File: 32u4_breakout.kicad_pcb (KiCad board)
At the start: 2 copper layers, 40 x 80 mm, 15 parts, among them J1 ICSP, J8 PWR, J9 GND, U1 ATmega32U4-A, Y1 16 MHz

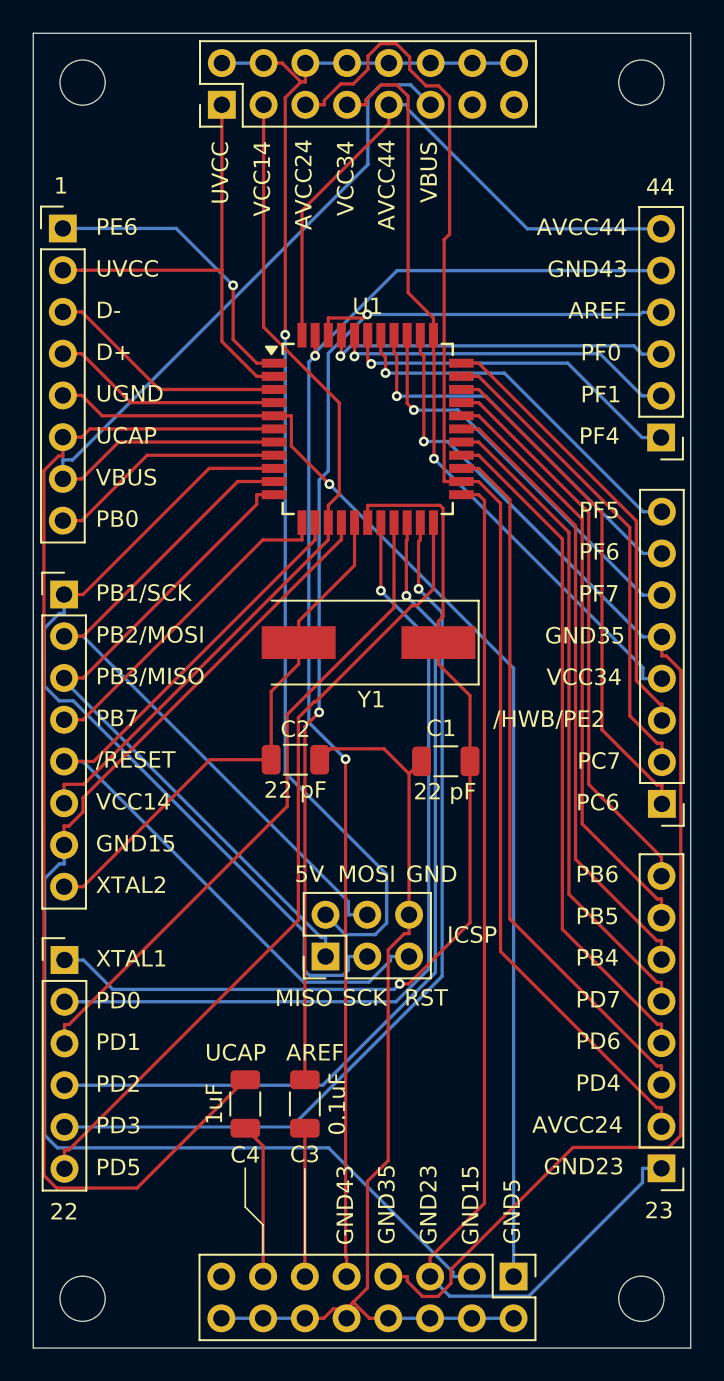
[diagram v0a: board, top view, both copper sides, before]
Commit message: Added LED for power and PC7/IO13
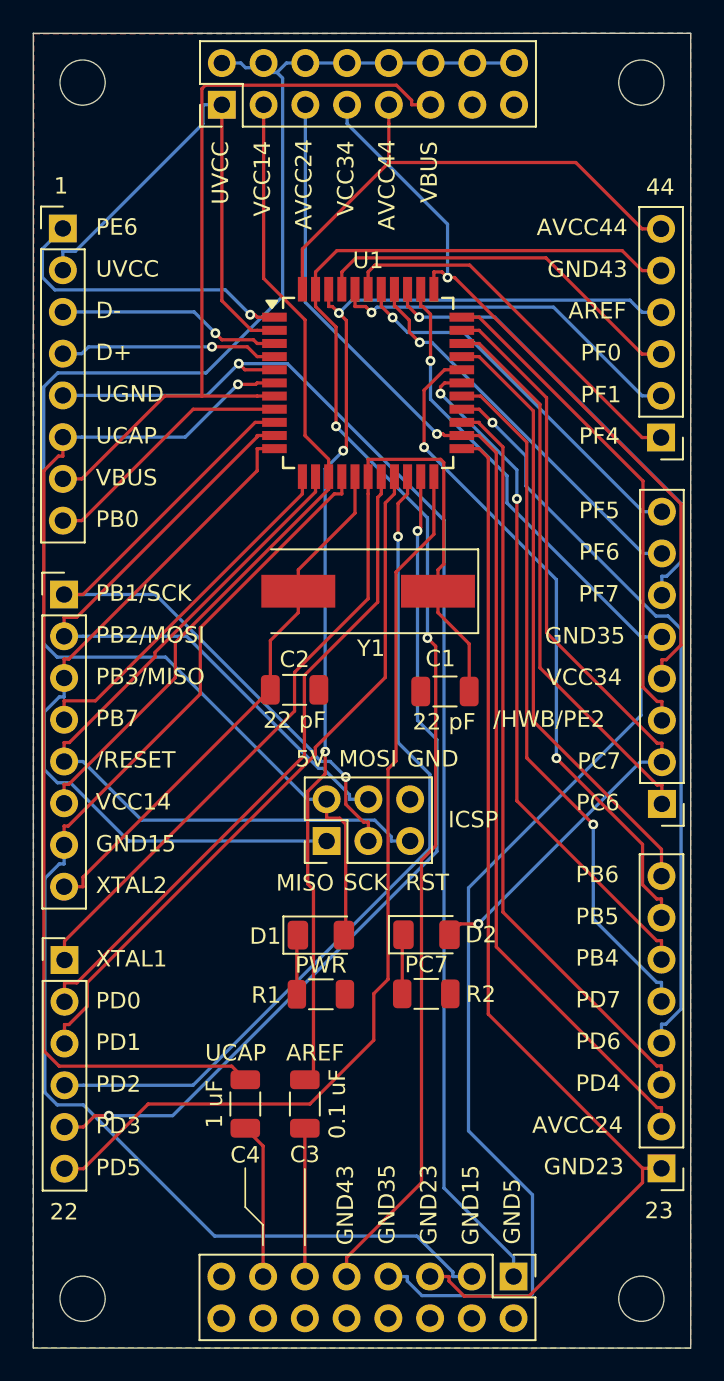
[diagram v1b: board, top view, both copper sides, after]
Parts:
- added D1: PWR, LED_SMD:LED_1206_3216Metric, F.Cu at (137.5, 94.9)
- added D2: PC7, LED_SMD:LED_1206_3216Metric, F.Cu at (143.9, 94.8)
- added R1: 220, Resistor_SMD:R_1206_3216Metric, F.Cu at (137.5, 98.5)
- added R2: 220, Resistor_SMD:R_1206_3216Metric, F.Cu at (143.9, 98.5)
- C3: value 0.1uF -> 0.1 uF
- C4: value 1uF -> 1 uF
- moved J1 7.03 mm to (137.8, 89.2)
- moved C1 4.25 mm to (145.1, 80.0)
- moved C2 4.25 mm to (135.9, 80.0)
- moved Y1 3.13 mm to (140.4, 74.0)
- moved U1 2.80 mm to (140.4, 61.3)
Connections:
- net Net-(J6-Pin_2) renamed IO13
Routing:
- net GND: track 60.3 -> 0.00 mm
- net IO13: track 29.3 -> 49.4 mm, vias 0 -> 1
- net 5V: track 78.1 -> 95.3 mm, vias 1 -> 0
- net Net-(J4-Pin_2): track 51.4 -> 40.4 mm, vias 1 -> 0
- net PWR24: track 82.4 -> 72.8 mm, vias 0 -> 1
- net Net-(J4-Pin_6): track 49.0 -> 57.9 mm
- net UCAP: track 73.9 -> 65.2 mm, vias 0 -> 1
- net SCK: track 51.5 -> 43.6 mm, vias 0 -> 1
- net GND43: track 81.7 -> 88.5 mm
- net GND5: track 72.4 -> 78.0 mm
- net Net-(J5-Pin_7): track 36.4 -> 41.1 mm, vias 0 -> 2
- net Net-(J6-Pin_6): track 24.5 -> 28.9 mm
- net PWR44: track 36.1 -> 31.6 mm
- net Net-(J5-Pin_4): track 41.6 -> 45.8 mm, vias 0 -> 1
- net Net-(J5-Pin_6): track 38.1 -> 42.0 mm, vias 0 -> 2
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- added copper zone on B.Cu, net GND
- added copper zone on F.Cu, net GND

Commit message: Fixed routing (missing grounds)
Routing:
- net GND: track 0.00 -> 85.5 mm
- net XTAL2: track 33.0 -> 63.8 mm
- net 5V: track 95.3 -> 77.1 mm, vias 0 -> 1
- net GND35: track 83.4 -> 73.6 mm
- net PWR34: track 46.2 -> 54.8 mm
- net SCK: track 43.6 -> 51.3 mm, vias 1 -> 0
- net GND15: track 76.3 -> 83.4 mm, vias 0 -> 1
- net PWR14: track 51.0 -> 57.4 mm, vias 0 -> 2
- net Net-(J3-Pin_4): track 21.9 -> 28.1 mm, vias 0 -> 1
- net UCAP: track 65.2 -> 59.5 mm
- net PWR24: track 72.8 -> 77.7 mm, vias 1 -> 0
- net AREF: track 70.2 -> 74.4 mm, vias 3 -> 1
- net VBUS: track 48.3 -> 51.8 mm
- net MISO: track 45.3 -> 41.9 mm
- net Net-(J4-Pin_4): track 51.9 -> 48.6 mm
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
